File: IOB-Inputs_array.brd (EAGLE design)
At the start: 106.7 x 104.1 mm, 92 parts

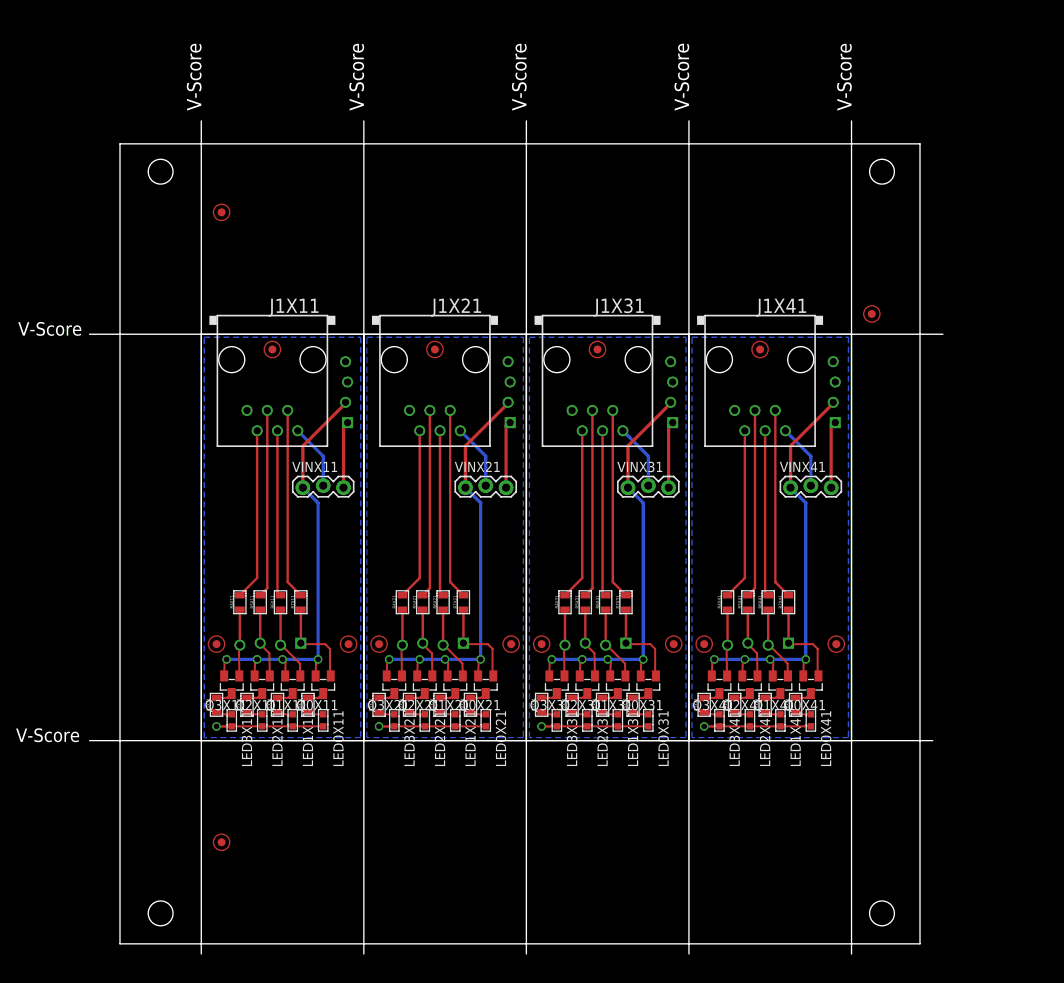
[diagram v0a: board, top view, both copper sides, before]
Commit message: Panelized
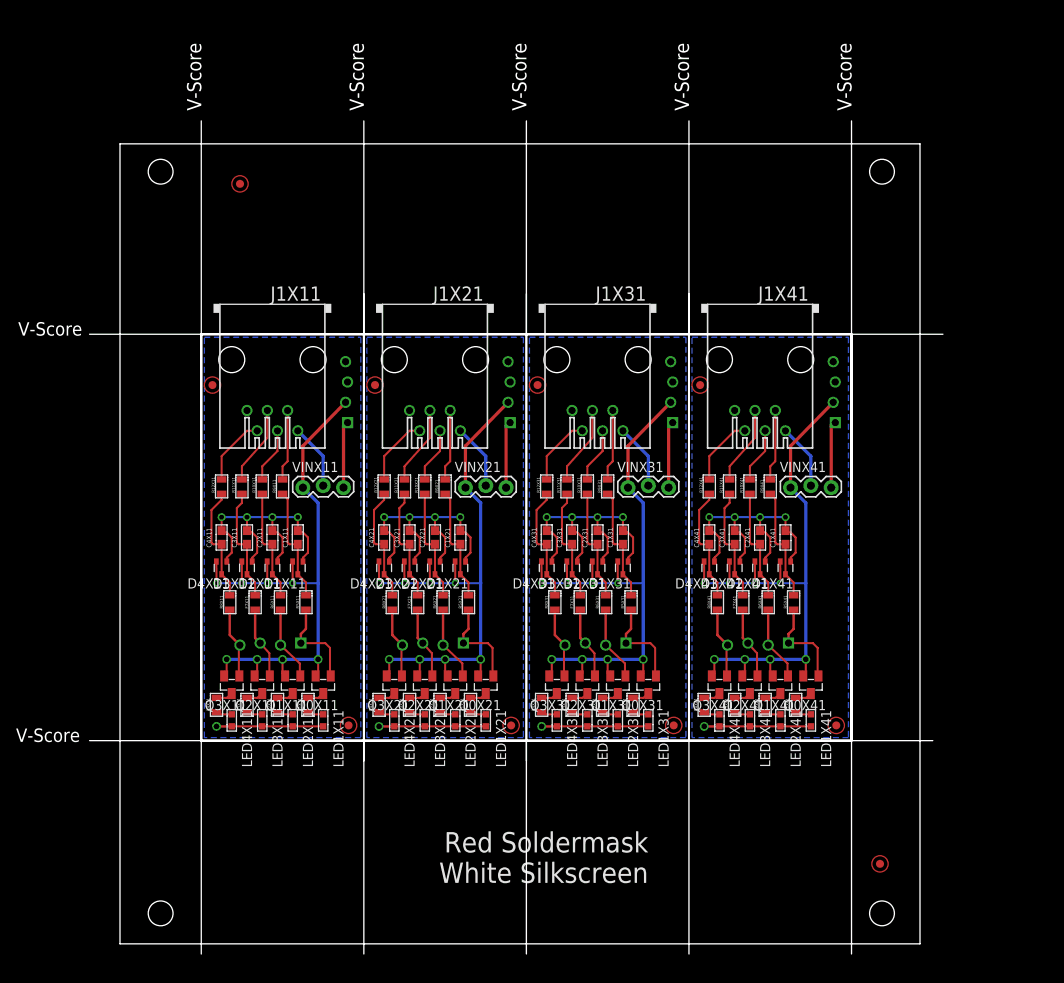
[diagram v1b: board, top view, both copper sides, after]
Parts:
- removed FID2, FID3X11, FID3X21, FID3X31, FID3X41: (no value), SPCoast:FIDUCIAL_1MM
- removed LED0X11, LED0X21, LED0X31, LED0X41: (no value), SPCoast:0603-LED
- removed R0X11, R0X21, R0X31, R0X41, R7X11, R7X21, R7X31, R7X41: (no value), SPCoast:0805-RES
- added C1X11, C1X21, C1X31, C1X41, C2X11, C2X21, C2X31, C2X41, C3X11, C3X21, C3X31, C3X41, C4X11, C4X21, C4X31, C4X41: (no value), SPCoast:0603-CAP
- added D1X11, D1X21, D1X31, D1X41, D2X11, D2X21, D2X31, D2X41, D3X11, D3X21, D3X31, D3X41, D4X11, D4X21, D4X31, D4X41: (no value), SPCoast:SOT323R
- added F7X11, F7X21, F7X31, F7X41, R10X11, R10X21, R10X31, R10X41, R11X11, R11X21, R11X31, R11X41, R12X11, R12X21, R12X31, R12X41, R8X11, R8X21, R8X31, R8X41, R9X11, R9X21, R9X31, R9X41: (no value), SPCoast:0805-RES
- added LED4X11, LED4X21, LED4X31, LED4X41: (no value), SPCoast:0603-LED
- J1X11, J1X21, J1X31, J1X41: device SPCoast:RJ25 -> SPCoast:RJ25-PANEL
- moved FID1 82.3 mm to (95.0, 10.0)
- moved R4X11 13.2 mm to (12.1, 29.8)
- moved R4X21 13.2 mm to (32.4, 29.8)
- moved R4X31 13.2 mm to (52.7, 29.8)
- moved R4X41 13.2 mm to (73.0, 29.8)
- moved FID2X11 10.2 mm to (28.6, 27.3)
- moved FID2X21 10.2 mm to (48.9, 27.3)
- moved FID2X31 10.2 mm to (69.2, 27.3)
- moved FID2X41 10.2 mm to (89.5, 27.3)
- moved FID1X41 8.71 mm to (72.5, 69.8)
- moved FID1X11 8.71 mm to (11.6, 69.8)
- moved FID1X21 8.71 mm to (31.9, 69.8)
- moved FID1X31 8.71 mm to (52.2, 69.8)
- moved R5X21 5.72 mm to (43.6, 42.7)
- moved R5X31 5.72 mm to (63.9, 42.7)
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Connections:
- new net N$10X11: C4X11.1, D4X11.2, R12X11.1, R8X11.2
- new net N$10X21: C4X21.1, D4X21.2, R12X21.1, R8X21.2
- new net N$10X31: C4X31.1, D4X31.2, R12X31.1, R8X31.2
- new net N$10X41: C4X41.1, D4X41.2, R12X41.1, R8X41.2
- new net N$12X11: C3X11.1, D3X11.2, F7X11.2, R11X11.1
- new net N$12X21: C3X21.1, D3X21.2, F7X21.2, R11X21.1
- new net N$12X31: C3X31.1, D3X31.2, F7X31.2, R11X31.1
- new net N$12X41: C3X41.1, D3X41.2, F7X41.2, R11X41.1
- new net N$13X11: C2X11.1, D2X11.2, R10X11.1, R6X11.2
- new net N$13X21: C2X21.1, D2X21.2, R10X21.1, R6X21.2
- new net N$13X31: C2X31.1, D2X31.2, R10X31.1, R6X31.2
- new net N$13X41: C2X41.1, D2X41.2, R10X41.1, R6X41.2
- new net N$14X11: C1X11.1, D1X11.2, R5X11.2, R9X11.1
- new net N$14X21: C1X21.1, D1X21.2, R5X21.2, R9X21.1
- new net N$14X31: C1X31.1, D1X31.2, R5X31.2, R9X31.1
- new net N$14X41: C1X41.1, D1X41.2, R5X41.2, R9X41.1
- net !IO1X11: now also R9X11.2; no longer R7X11.2
- net !IO1X21: now also R9X21.2; no longer R7X21.2
- net !IO1X31: now also R9X31.2; no longer R7X31.2
- net !IO1X41: now also R9X41.2; no longer R7X41.2
- net !IO2X11: now also R10X11.2; no longer R6X11.2
- net !IO2X21: now also R10X21.2; no longer R6X21.2
- net !IO2X31: now also R10X31.2; no longer R6X31.2
- net !IO2X41: now also R10X41.2; no longer R6X41.2
- net !IO3X11: now also R11X11.2; no longer R5X11.2
- net !IO3X21: now also R11X21.2; no longer R5X21.2
- net !IO3X31: now also R11X31.2; no longer R5X31.2
- net !IO3X41: now also R11X41.2; no longer R5X41.2
- net !IO4X11: now also R12X11.2; no longer R4X11.2
- net !IO4X21: now also R12X21.2; no longer R4X21.2
- net !IO4X31: now also R12X31.2; no longer R4X31.2
- net !IO4X41: now also R12X41.2; no longer R4X41.2
- net GNDX11: now also C1X11.2, C2X11.2, C3X11.2, C4X11.2, D1X11.1, D2X11.1, D3X11.1, D4X11.1, LED4X11.C; no longer LED0X11.C
- net GNDX21: now also C1X21.2, C2X21.2, C3X21.2, C4X21.2, D1X21.1, D2X21.1, D3X21.1, D4X21.1, LED4X21.C; no longer LED0X21.C
- net GNDX31: now also C1X31.2, C2X31.2, C3X31.2, C4X31.2, D1X31.1, D2X31.1, D3X31.1, D4X31.1, LED4X31.C; no longer LED0X31.C
- net GNDX41: now also C1X41.2, C2X41.2, C3X41.2, C4X41.2, D1X41.1, D2X41.1, D3X41.1, D4X41.1, LED4X41.C; no longer LED0X41.C
- net N$11X11: now also R1X11.2; no longer R0X11.2
- net N$11X21: now also R1X21.2; no longer R0X21.2
- net N$11X31: now also R1X31.2; no longer R0X31.2
- net N$11X41: now also R1X41.2; no longer R0X41.2
- net N$2X11: now also LED1X11.A, R1X11.1; no longer LED0X11.A, R0X11.1
- net N$2X21: now also LED1X21.A, R1X21.1; no longer LED0X21.A, R0X21.1
- net N$2X31: now also LED1X31.A, R1X31.1; no longer LED0X31.A, R0X31.1
- net N$2X41: now also LED1X41.A, R1X41.1; no longer LED0X41.A, R0X41.1
- net N$30X11: now also R2X11.2; no longer R1X11.2
- net N$30X21: now also R2X21.2; no longer R1X21.2
- net N$30X31: now also R2X31.2; no longer R1X31.2
- net N$30X41: now also R2X41.2; no longer R1X41.2
- net N$31X11: now also R3X11.2; no longer R2X11.2
- net N$31X21: now also R3X21.2; no longer R2X21.2
- net N$31X31: now also R3X31.2; no longer R2X31.2
- net N$31X41: now also R3X41.2; no longer R2X41.2
- net N$32X11: now also R4X11.2; no longer R3X11.2
- net N$32X21: now also R4X21.2; no longer R3X21.2
- net N$32X31: now also R4X31.2; no longer R3X31.2
- net N$32X41: now also R4X41.2; no longer R3X41.2
- net N$3X11: now also LED2X11.A, R2X11.1; no longer LED1X11.A, R1X11.1
- net N$3X21: now also LED2X21.A, R2X21.1; no longer LED1X21.A, R1X21.1
- net N$3X31: now also LED2X31.A, R2X31.1; no longer LED1X31.A, R1X31.1
- net N$3X41: now also LED2X41.A, R2X41.1; no longer LED1X41.A, R1X41.1
- net N$4X11: now also LED3X11.A, R3X11.1; no longer LED2X11.A, R2X11.1
- net N$4X21: now also LED3X21.A, R3X21.1; no longer LED2X21.A, R2X21.1
- net N$4X31: now also LED3X31.A, R3X31.1; no longer LED2X31.A, R2X31.1
- net N$4X41: now also LED3X41.A, R3X41.1; no longer LED2X41.A, R2X41.1
- net N$5X11: now also LED4X11.A, R4X11.1; no longer LED3X11.A, R3X11.1
- net N$5X21: now also LED4X21.A, R4X21.1; no longer LED3X21.A, R3X21.1
- net N$5X31: now also LED4X31.A, R4X31.1; no longer LED3X31.A, R3X31.1
- net N$5X41: now also LED4X41.A, R4X41.1; no longer LED3X41.A, R3X41.1
- net P1X11: now also R5X11.1; no longer R7X11.1
- net P1X21: now also R5X21.1; no longer R7X21.1
- net P1X31: now also R5X31.1; no longer R7X31.1
- net P1X41: now also R5X41.1; no longer R7X41.1
- net P3X11: now also F7X11.1; no longer R5X11.1
- net P3X21: now also F7X21.1; no longer R5X21.1
- net P3X31: now also F7X31.1; no longer R5X31.1
- net P3X41: now also F7X41.1; no longer R5X41.1
- net P4X11: now also R8X11.1; no longer R4X11.1
- net P4X21: now also R8X21.1; no longer R4X21.1
- net P4X31: now also R8X31.1; no longer R4X31.1
- net P4X41: now also R8X41.1; no longer R4X41.1
- net VCCX11: now also D1X11.3, D2X11.3, D3X11.3, D4X11.3
- net VCCX21: now also D1X21.3, D2X21.3, D3X21.3, D4X21.3
- net VCCX31: now also D1X31.3, D2X31.3, D3X31.3, D4X31.3
- net VCCX41: now also D1X41.3, D2X41.3, D3X41.3, D4X41.3
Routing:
- net GNDX41: track 13.3 -> 49.2 mm, vias 1 -> 5
- net GNDX31: track 13.3 -> 49.2 mm, vias 1 -> 5
- net GNDX21: track 13.3 -> 49.2 mm, vias 1 -> 5
- net GNDX11: track 13.3 -> 49.2 mm, vias 1 -> 5
- net VCCX31: track 55.4 -> 79.2 mm, vias 4 -> 8
- net VCCX21: track 55.4 -> 79.2 mm, vias 4 -> 8
- net VCCX11: track 55.4 -> 79.2 mm, vias 4 -> 8
- net VCCX41: track 55.4 -> 79.2 mm, vias 4 -> 8
- net !IO1X31: track 23.8 -> 8.89 mm
- net !IO1X21: track 23.8 -> 8.89 mm
- net !IO1X11: track 23.8 -> 8.89 mm
- net !IO1X41: track 23.8 -> 8.89 mm
- net N$10X31: track 0.00 -> 14.8 mm
- net N$10X21: track 0.00 -> 14.8 mm
- net N$10X11: track 0.00 -> 14.8 mm
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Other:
- board text added: "1.3"
- board text added: "15, 95"
- board text added: "95, 10"
- board text added: "C1"
- board text added: "C2"
- board text added: "C3"
- board text added: "C4"
- board text added: "D1"
- board text added: "D2"
- board text added: "D3"
- board text added: "D4"
- board text added: "F7"
- board text added: "J1"
- board text added: "Q0"
- board text added: "Q1"
- board text added: "Q2"
- board text added: "Q3"
- board text added: "R1"
- board text added: "R10"
- board text added: "R11"
- board text added: "R12"
- board text added: "R2"
- board text added: "R3"
- board text added: "R4"
- board text added: "R5"
- board text added: "R6"
- board text added: "R8"
- board text added: "R9"
- board text added: "Red Soldermask White Silkscreen"
- board text added: "V1.3 2019-12"
- board text added: "VIN"
- board text removed: "(aka 1.0C)"
- board text removed: "(aka V1.0C)"
- board text removed: "1.2"
- board text removed: "12.7, 12.7"
- board text removed: "12.7, 91.44"
- board text removed: "3700, 3100"
- board text removed: "500, 3600"
- board text removed: "500, 500"
- board text removed: "93.98, 78.74"
- board text removed: "V1.2 2018-01"

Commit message: added 1x6 0.100 header
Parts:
- added CON1X11, CON1X21, CON1X31, CON1X41: (no value), SPCoast:1X06_LOCK
- moved FID1X41 7.75 mm to (78.9, 74.3)
- moved FID1X11 7.75 mm to (17.9, 74.3)
- moved FID1X21 7.75 mm to (38.2, 74.3)
- moved FID1X31 7.75 mm to (58.5, 74.3)
- renumbered F7X11 to R7X11, F7X21 to R7X21, F7X31 to R7X31, F7X41 to R7X41
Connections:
- net !IO1X11: now also CON1X11.2
- net !IO1X21: now also CON1X21.2
- net !IO1X31: now also CON1X31.2
- net !IO1X41: now also CON1X41.2
- net !IO2X11: now also CON1X11.3
- net !IO2X21: now also CON1X21.3
- net !IO2X31: now also CON1X31.3
- net !IO2X41: now also CON1X41.3
- net !IO3X11: now also CON1X11.4
- net !IO3X21: now also CON1X21.4
- net !IO3X31: now also CON1X31.4
- net !IO3X41: now also CON1X41.4
- net !IO4X11: now also CON1X11.5
- net !IO4X21: now also CON1X21.5
- net !IO4X31: now also CON1X31.5
- net !IO4X41: now also CON1X41.5
- net GNDX11: now also CON1X11.6
- net GNDX21: now also CON1X21.6
- net GNDX31: now also CON1X31.6
- net GNDX41: now also CON1X41.6
- net N$1X11: now also CON1X11.1
- net N$1X21: now also CON1X21.1
- net N$1X31: now also CON1X31.1
- net N$1X41: now also CON1X41.1
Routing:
- net N$1X31: track 8.17 -> 14.6 mm
- net N$1X41: track 8.17 -> 14.6 mm
- net N$1X21: track 8.17 -> 14.6 mm
- net N$1X11: track 8.17 -> 14.6 mm
- net !IO4X41: track 8.67 -> 14.5 mm
- net !IO4X21: track 8.67 -> 14.5 mm
- net !IO4X11: track 8.67 -> 14.5 mm
- net !IO4X31: track 8.67 -> 14.5 mm
- net !IO2X41: track 6.87 -> 12.2 mm
- net !IO2X11: track 6.87 -> 12.2 mm
- net !IO2X31: track 6.87 -> 12.2 mm
- net !IO2X21: track 6.87 -> 12.2 mm
- net !IO1X31: track 8.89 -> 12.5 mm
- net !IO1X21: track 8.89 -> 12.5 mm
- net !IO1X11: track 8.89 -> 12.5 mm
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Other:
- board text added: "1.4"
- board text added: "R7"
- board text added: "V1.4 2020-01"
- board text removed: "1.3"
- board text removed: "F7"
- board text removed: "J1"
- board text removed: "V1.3 2019-12"
- board text removed: "VIN"

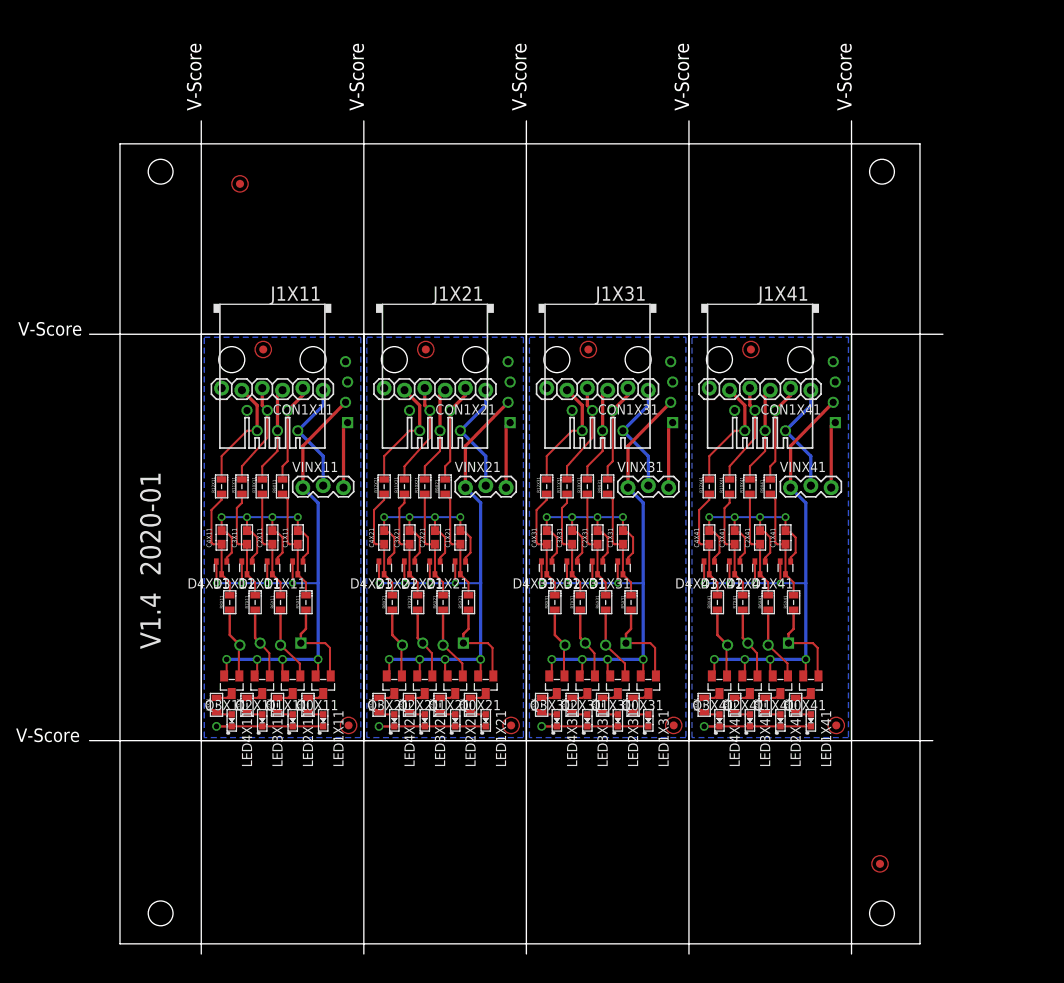
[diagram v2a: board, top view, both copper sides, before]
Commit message: new IOB design
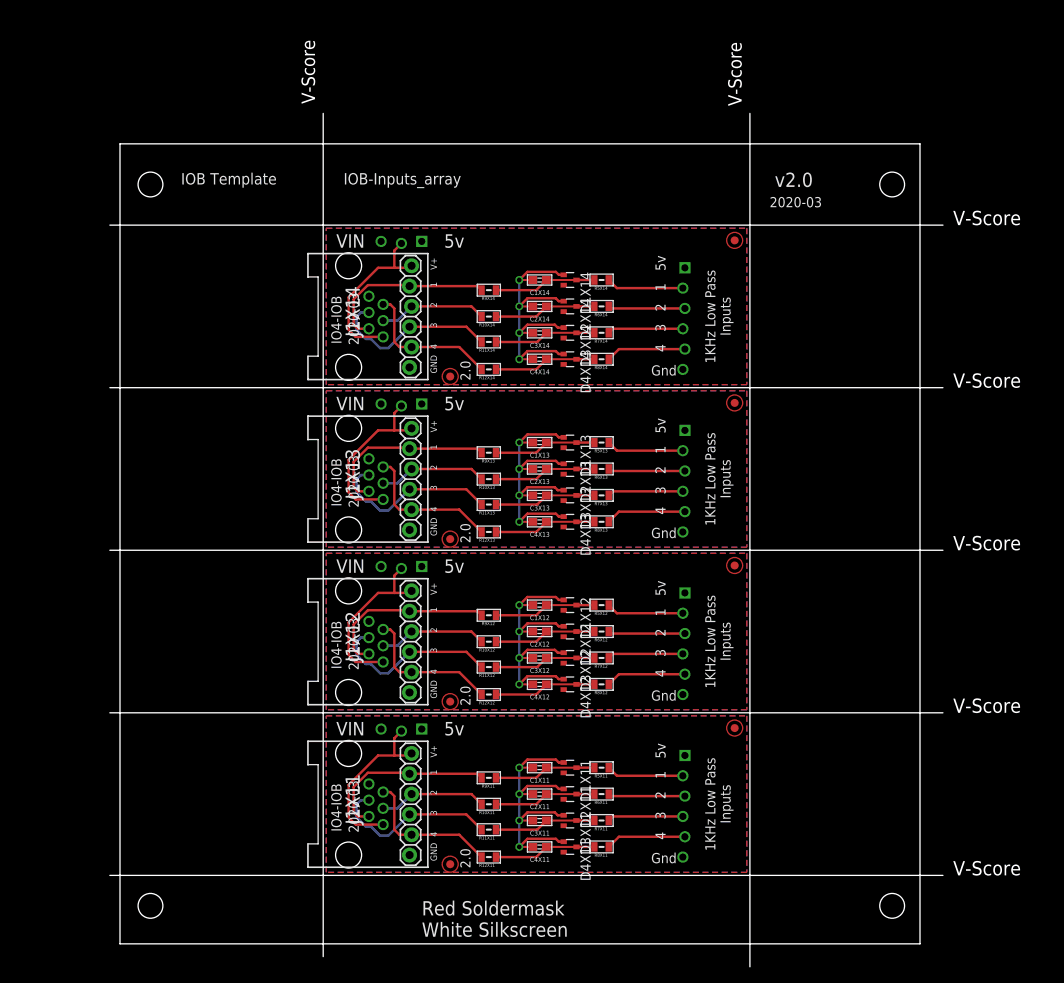
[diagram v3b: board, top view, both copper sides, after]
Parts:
- removed C1X21, C1X31, C1X41, C2X21, C2X31, C2X41, C3X21, C3X31, C3X41, C4X21, C4X31, C4X41: (no value), SPCoast:0603-CAP
- removed CON1X11, CON1X21, CON1X31, CON1X41: (no value), SPCoast:1X06_LOCK
- removed D1X21, D1X31, D1X41, D2X21, D2X31, D2X41, D3X21, D3X31, D3X41, D4X21, D4X31, D4X41: (no value), SPCoast:SOT323R
- removed FID1, FID1X21, FID1X31, FID1X41, FID2X21, FID2X31, FID2X41, FID3: (no value), SPCoast:FIDUCIAL_1MM
- removed IOBX21, IOBX31, IOBX41: (no value), SPCoast:IO4-IOB
- removed J1X21, J1X31, J1X41: (no value), SPCoast:RJ25-PANEL
- removed LED1X11, LED1X21, LED1X31, LED1X41, LED2X11, LED2X21, LED2X31, LED2X41, LED3X11, LED3X21, LED3X31, LED3X41, LED4X11, LED4X21, LED4X31, LED4X41: (no value), SPCoast:0603-LED
- removed Q0X11, Q0X21, Q0X31, Q0X41, Q1X11, Q1X21, Q1X31, Q1X41, Q2X11, Q2X21, Q2X31, Q2X41, Q3X11, Q3X21, Q3X31, Q3X41: (no value), SPCoast:SOT23
- removed R10X21, R10X31, R10X41, R11X21, R11X31, R11X41, R12X21, R12X31, R12X41, R1X11, R1X21, R1X31, R1X41, R2X11, R2X21, R2X31, R2X41, R3X11, R3X21, R3X31, R3X41, R4X11, R4X21, R4X31, R4X41, R5X21, R5X31, R5X41, R6X21, R6X31, R6X41, R7X21, R7X31, R7X41, R8X21, R8X31, R8X41, R9X21, R9X31, R9X41: (no value), SPCoast:0805-RES
- removed VINX1: (no value), SPCoast:BOARD-DINRAIL-3.17IN-4X-IOB
- removed VINX11, VINX21, VINX31, VINX41: (no value), SPCoast:1X03
- added C1X12, C1X13, C1X14, C2X12, C2X13, C2X14, C3X12, C3X13, C3X14, C4X12, C4X13, C4X14: (no value), SPCoast:0603-CAP
- added D1X12, D1X13, D1X14, D2X12, D2X13, D2X14, D3X12, D3X13, D3X14, D4X12, D4X13, D4X14: (no value), SPCoast:SOT323R
- added FID1X12, FID1X13, FID1X14, FID2X12, FID2X13, FID2X14: (no value), SPCoast:FIDUCIAL_1MM
- added IOBX12, IOBX13, IOBX14: (no value), SPCoast:IO4-IOB
- added J1X12, J1X13, J1X14: (no value), SPCoast:RJ24-INVERTED-PINS
- added R10X12, R10X13, R10X14, R11X12, R11X13, R11X14, R12X12, R12X13, R12X14, R5X12, R5X13, R5X14, R6X12, R6X13, R6X14, R7X12, R7X13, R7X14, R8X12, R8X13, R8X14, R9X12, R9X13, R9X14: (no value), SPCoast:0805-RES
- added R12X1: (no value), SPCoast:BOARD-DINRAIL-3.17IN-H4X-IOB
- J1X11: device SPCoast:RJ25-PANEL -> SPCoast:RJ24-INVERTED-PINS
- moved IOBX11 69.3 mm to (25.4, 8.56), turned to 0 degrees
- moved FID1X11 68.5 mm to (41.3, 9.96), turned to 0 degrees
- moved J1X11 57.2 mm to (32.4, 17.4), turned to 90 degrees
- moved R12X11 57.1 mm to (46.1, 10.8), turned to 180 degrees
- moved D4X11 55.8 mm to (56.3, 12.1), turned to 270 degrees
- moved R8X11 55.6 mm to (60.2, 12.1), turned to 180 degrees
- moved C4X11 55.5 mm to (52.5, 12.1), turned to 180 degrees
- moved R11X11 52.8 mm to (46.1, 14.3), turned to 180 degrees
- moved D3X11 51.3 mm to (56.3, 15.4), turned to 270 degrees
- moved R7X11 51.2 mm to (60.2, 15.4), turned to 180 degrees
- moved C3X11 50.9 mm to (52.5, 15.4), turned to 180 degrees
- moved R10X11 48.8 mm to (46.1, 17.4), turned to 180 degrees
- moved FID2X11 48.3 mm to (76.8, 27.0), turned to 0 degrees
- moved R6X11 46.7 mm to (60.2, 18.7), turned to 180 degrees
- moved D2X11 46.7 mm to (56.3, 18.7), turned to 270 degrees
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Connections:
- removed net !IO1X21: CON1X21.2, J1X21.2, R9X21.2
- removed net !IO1X31: CON1X31.2, J1X31.2, R9X31.2
- removed net !IO1X41: CON1X41.2, J1X41.2, R9X41.2
- removed net !IO2X21: CON1X21.3, J1X21.3, R10X21.2
- removed net !IO2X31: CON1X31.3, J1X31.3, R10X31.2
- removed net !IO2X41: CON1X41.3, J1X41.3, R10X41.2
- removed net !IO3X21: CON1X21.4, J1X21.4, R11X21.2
- removed net !IO3X31: CON1X31.4, J1X31.4, R11X31.2
- removed net !IO3X41: CON1X41.4, J1X41.4, R11X41.2
- removed net !IO4X21: CON1X21.5, J1X21.5, R12X21.2
- removed net !IO4X31: CON1X31.5, J1X31.5, R12X31.2
- removed net !IO4X41: CON1X41.5, J1X41.5, R12X41.2
- removed net GNDX21: C1X21.2, C2X21.2, C3X21.2, C4X21.2, CON1X21.6, D1X21.1, D2X21.1, D3X21.1, D4X21.1, IOBX21.G@1, IOBX21.G@2, J1X21.6, LED1X21.C, LED2X21.C, LED3X21.C, LED4X21.C
- removed net GNDX31: C1X31.2, C2X31.2, C3X31.2, C4X31.2, CON1X31.6, D1X31.1, D2X31.1, D3X31.1, D4X31.1, IOBX31.G@1, IOBX31.G@2, J1X31.6, LED1X31.C, LED2X31.C, LED3X31.C, LED4X31.C
- removed net GNDX41: C1X41.2, C2X41.2, C3X41.2, C4X41.2, CON1X41.6, D1X41.1, D2X41.1, D3X41.1, D4X41.1, IOBX41.G@1, IOBX41.G@2, J1X41.6, LED1X41.C, LED2X41.C, LED3X41.C, LED4X41.C
- removed net N$10X21: C4X21.1, D4X21.2, R12X21.1, R8X21.2
- removed net N$10X31: C4X31.1, D4X31.2, R12X31.1, R8X31.2
- removed net N$10X41: C4X41.1, D4X41.2, R12X41.1, R8X41.2
- removed net N$11X11: Q0X11.3, R1X11.2
- removed net N$11X21: Q0X21.3, R1X21.2
- removed net N$11X31: Q0X31.3, R1X31.2
- removed net N$11X41: Q0X41.3, R1X41.2
- removed net N$12X21: C3X21.1, D3X21.2, R11X21.1, R7X21.2
- removed net N$12X31: C3X31.1, D3X31.2, R11X31.1, R7X31.2
- removed net N$12X41: C3X41.1, D3X41.2, R11X41.1, R7X41.2
- removed net N$13X21: C2X21.1, D2X21.2, R10X21.1, R6X21.2
- removed net N$13X31: C2X31.1, D2X31.2, R10X31.1, R6X31.2
- removed net N$13X41: C2X41.1, D2X41.2, R10X41.1, R6X41.2
- removed net N$14X21: C1X21.1, D1X21.2, R5X21.2, R9X21.1
- removed net N$14X31: C1X31.1, D1X31.2, R5X31.2, R9X31.1
- removed net N$14X41: C1X41.1, D1X41.2, R5X41.2, R9X41.1
- removed net N$1X11: CON1X11.1, J1X11.1, VINX11.2
- removed net N$1X21: CON1X21.1, J1X21.1, VINX21.2
- removed net N$1X31: CON1X31.1, J1X31.1, VINX31.2
- removed net N$1X41: CON1X41.1, J1X41.1, VINX41.2
- removed net N$2X11: LED1X11.A, R1X11.1
- removed net N$2X21: LED1X21.A, R1X21.1
- removed net N$2X31: LED1X31.A, R1X31.1
- removed net N$2X41: LED1X41.A, R1X41.1
- removed net N$30X11: Q1X11.3, R2X11.2
- removed net N$30X21: Q1X21.3, R2X21.2
- removed net N$30X31: Q1X31.3, R2X31.2
- removed net N$30X41: Q1X41.3, R2X41.2
- removed net N$31X11: Q2X11.3, R3X11.2
- removed net N$31X21: Q2X21.3, R3X21.2
- removed net N$31X31: Q2X31.3, R3X31.2
- removed net N$31X41: Q2X41.3, R3X41.2
- removed net N$32X11: Q3X11.3, R4X11.2
- removed net N$32X21: Q3X21.3, R4X21.2
- removed net N$32X31: Q3X31.3, R4X31.2
- removed net N$32X41: Q3X41.3, R4X41.2
- removed net N$3X11: LED2X11.A, R2X11.1
- removed net N$3X21: LED2X21.A, R2X21.1
- removed net N$3X31: LED2X31.A, R2X31.1
- removed net N$3X41: LED2X41.A, R2X41.1
- removed net N$4X11: LED3X11.A, R3X11.1
- removed net N$4X21: LED3X21.A, R3X21.1
- removed net N$4X31: LED3X31.A, R3X31.1
- removed net N$4X41: LED3X41.A, R3X41.1
- removed net N$5X11: LED4X11.A, R4X11.1
- removed net N$5X21: LED4X21.A, R4X21.1
- removed net N$5X31: LED4X31.A, R4X31.1
- removed net N$5X41: LED4X41.A, R4X41.1
- removed net P1X21: IOBX21.P1, Q0X21.1, R5X21.1
- removed net P1X31: IOBX31.P1, Q0X31.1, R5X31.1
- removed net P1X41: IOBX41.P1, Q0X41.1, R5X41.1
- removed net P2X21: IOBX21.P2, Q1X21.1, R6X21.1
- removed net P2X31: IOBX31.P2, Q1X31.1, R6X31.1
- removed net P2X41: IOBX41.P2, Q1X41.1, R6X41.1
- removed net P3X21: IOBX21.P3, Q2X21.1, R7X21.1
- removed net P3X31: IOBX31.P3, Q2X31.1, R7X31.1
- removed net P3X41: IOBX41.P3, Q2X41.1, R7X41.1
- removed net P4X21: IOBX21.P4, Q3X21.1, R8X21.1
- removed net P4X31: IOBX31.P4, Q3X31.1, R8X31.1
- removed net P4X41: IOBX41.P4, Q3X41.1, R8X41.1
- removed net VCCIOX21: IOBX21.V+, VINX21.3
- removed net VCCIOX31: IOBX31.V+, VINX31.3
- removed net VCCIOX41: IOBX41.V+, VINX41.3
- removed net VCCX21: D1X21.3, D2X21.3, D3X21.3, D4X21.3, IOBX21.V5, Q0X21.2, Q1X21.2, Q2X21.2, Q3X21.2, VINX21.1
- removed net VCCX31: D1X31.3, D2X31.3, D3X31.3, D4X31.3, IOBX31.V5, Q0X31.2, Q1X31.2, Q2X31.2, Q3X31.2, VINX31.1
- removed net VCCX41: D1X41.3, D2X41.3, D3X41.3, D4X41.3, IOBX41.V5, Q0X41.2, Q1X41.2, Q2X41.2, Q3X41.2, VINX41.1
- new net !IO1X12: J1X12.2, J1X12.2@1, R9X12.2
- new net !IO1X13: J1X13.2, J1X13.2@1, R9X13.2
- new net !IO1X14: J1X14.2, J1X14.2@1, R9X14.2
- new net !IO2X12: J1X12.3, J1X12.3@1, R10X12.2
- new net !IO2X13: J1X13.3, J1X13.3@1, R10X13.2
- new net !IO2X14: J1X14.3, J1X14.3@1, R10X14.2
- new net !IO3X12: J1X12.4, J1X12.4@1, R11X12.2
- new net !IO3X13: J1X13.4, J1X13.4@1, R11X13.2
- new net !IO3X14: J1X14.4, J1X14.4@1, R11X14.2
- new net !IO4X12: J1X12.5, J1X12.5@1, R12X12.2
- new net !IO4X13: J1X13.5, J1X13.5@1, R12X13.2
- new net !IO4X14: J1X14.5, J1X14.5@1, R12X14.2
- new net GNDX12: C1X12.2, C2X12.2, C3X12.2, C4X12.2, D1X12.1, D2X12.1, D3X12.1, D4X12.1, IOBX12.G@3, J1X12.6, J1X12.6@1
- new net GNDX13: C1X13.2, C2X13.2, C3X13.2, C4X13.2, D1X13.1, D2X13.1, D3X13.1, D4X13.1, IOBX13.G@3, J1X13.6, J1X13.6@1
- new net GNDX14: C1X14.2, C2X14.2, C3X14.2, C4X14.2, D1X14.1, D2X14.1, D3X14.1, D4X14.1, IOBX14.G@3, J1X14.6, J1X14.6@1
- new net N$10X12: C4X12.1, D4X12.2, R12X12.1, R8X12.2
- new net N$10X13: C4X13.1, D4X13.2, R12X13.1, R8X13.2
- new net N$10X14: C4X14.1, D4X14.2, R12X14.1, R8X14.2
- new net N$12X12: C3X12.1, D3X12.2, R11X12.1, R7X12.2
- new net N$12X13: C3X13.1, D3X13.2, R11X13.1, R7X13.2
- new net N$12X14: C3X14.1, D3X14.2, R11X14.1, R7X14.2
- new net N$13X12: C2X12.1, D2X12.2, R10X12.1, R6X12.2
- new net N$13X13: C2X13.1, D2X13.2, R10X13.1, R6X13.2
- new net N$13X14: C2X14.1, D2X14.2, R10X14.1, R6X14.2
- new net N$14X12: C1X12.1, D1X12.2, R5X12.2, R9X12.1
- new net N$14X13: C1X13.1, D1X13.2, R5X13.2, R9X13.1
- new net N$14X14: C1X14.1, D1X14.2, R5X14.2, R9X14.1
- new net P1X12: IOBX12.P1, R5X12.1
- new net P1X13: IOBX13.P1, R5X13.1
- new net P1X14: IOBX14.P1, R5X14.1
- new net P2X12: IOBX12.P2, R6X12.1
- new net P2X13: IOBX13.P2, R6X13.1
- new net P2X14: IOBX14.P2, R6X14.1
- new net P3X12: IOBX12.P3, R7X12.1
- new net P3X13: IOBX13.P3, R7X13.1
- new net P3X14: IOBX14.P3, R7X14.1
- new net P4X12: IOBX12.P4, R8X12.1
- new net P4X13: IOBX13.P4, R8X13.1
- new net P4X14: IOBX14.P4, R8X14.1
- new net VCCIOX12: IOBX12.V+
- new net VCCIOX13: IOBX13.V+
- new net VCCIOX14: IOBX14.V+
- new net VCCX12: D1X12.3, D2X12.3, D3X12.3, D4X12.3, IOBX12.V5, IOBX12.V5@1
- new net VCCX13: D1X13.3, D2X13.3, D3X13.3, D4X13.3, IOBX13.V5, IOBX13.V5@1
- new net VCCX14: D1X14.3, D2X14.3, D3X14.3, D4X14.3, IOBX14.V5, IOBX14.V5@1
- new net VOUTX11: IOBX11.VOUT, J1X11.1, J1X11.1@1
- new net VOUTX12: IOBX12.VOUT, J1X12.1, J1X12.1@1
- new net VOUTX13: IOBX13.VOUT, J1X13.1, J1X13.1@1
- new net VOUTX14: IOBX14.VOUT, J1X14.1, J1X14.1@1
- net !IO1X11: now also J1X11.2@1; no longer CON1X11.2
- net !IO2X11: now also J1X11.3@1; no longer CON1X11.3
- net !IO3X11: now also J1X11.4@1; no longer CON1X11.4
- net !IO4X11: now also J1X11.5@1; no longer CON1X11.5
- net GNDX11: now also IOBX11.G@3, J1X11.6@1; no longer CON1X11.6, IOBX11.G@1, IOBX11.G@2, LED1X11.C, LED2X11.C, LED3X11.C, LED4X11.C
- net P1X11: no longer Q0X11.1
- net P2X11: no longer Q1X11.1
- net P3X11: no longer Q2X11.1
- net P4X11: no longer Q3X11.1
- net VCCIOX11: no longer VINX11.3
- net VCCX11: now also IOBX11.V5@1; no longer Q0X11.2, Q1X11.2, Q2X11.2, Q3X11.2, VINX11.1
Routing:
- net VCCX31: track 79.2 -> 0.00 mm, vias 8 -> 0
- net VCCX21: track 79.2 -> 0.00 mm, vias 8 -> 0
- net VCCX11: track 79.2 -> 0.00 mm, vias 8 -> 0
- net VCCX41: track 79.2 -> 0.00 mm, vias 8 -> 0
- net GNDX41: track 49.2 -> 0.00 mm, vias 5 -> 0
- net GNDX31: track 49.2 -> 0.00 mm, vias 5 -> 0
- net GNDX21: track 49.2 -> 0.00 mm, vias 5 -> 0
- net GNDX14: track 0.00 -> 41.2 mm, vias 0 -> 4
- net GNDX13: track 0.00 -> 41.2 mm, vias 0 -> 4
- net GNDX12: track 0.00 -> 41.2 mm, vias 0 -> 4
- net !IO1X14: track 0.00 -> 22.3 mm
- net !IO1X13: track 0.00 -> 22.3 mm
- net !IO1X12: track 0.00 -> 22.3 mm
- net !IO3X13: track 0.00 -> 21.8 mm
- net !IO3X12: track 0.00 -> 21.8 mm
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- added copper zone on layer 16, net GNDX12
- added copper zone on layer 16, net GNDX13
- added copper zone on layer 16, net GNDX14
- added copper zone on layer 1, net VCCX11
- added copper zone on layer 1, net VCCX12
- added copper zone on layer 1, net VCCX13
- added copper zone on layer 1, net VCCX14
- removed copper zone on layer 16, net GNDX21
- removed copper zone on layer 16, net GNDX31
- removed copper zone on layer 16, net GNDX41
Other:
- board size 106.7 x 104.1 mm -> 104.1 x 106.7 mm
- board text added: "1KHz Low Pass"
- board text added: "2.0"
- board text added: "2020-03"
- board text added: "v2.0"
- board text removed: "1"
- board text removed: "1.4"
- board text removed: "15, 95"
- board text removed: "2"
- board text removed: "3"
- board text removed: "4"
- board text removed: "5v"
- board text removed: "95, 10"
- board text removed: "9v"
- board text removed: "IO4 Power"
- board text removed: "IOB Inputs"
- board text removed: "IOB to IO4 Interface"
- board text removed: "Made in the PCR, Coast Div, NMRA"
- board text removed: "Model Railroading is Fun!"
- board text removed: "Q0"
- board text removed: "Q1"
- board text removed: "Q2"
- board text removed: "Q3"
- board text removed: "R1"
- board text removed: "R2"
- board text removed: "R3"
- board text removed: "R4"
- board text removed: "SPCoast.com John Plocher"
- board text removed: "V1.4 2020-01"
